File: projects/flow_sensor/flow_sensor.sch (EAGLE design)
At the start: 89 parts, among them IC1 TPS61200, IC2 TPS61200, IC3 MIC5219BM5, J5 455-1750-1-ND

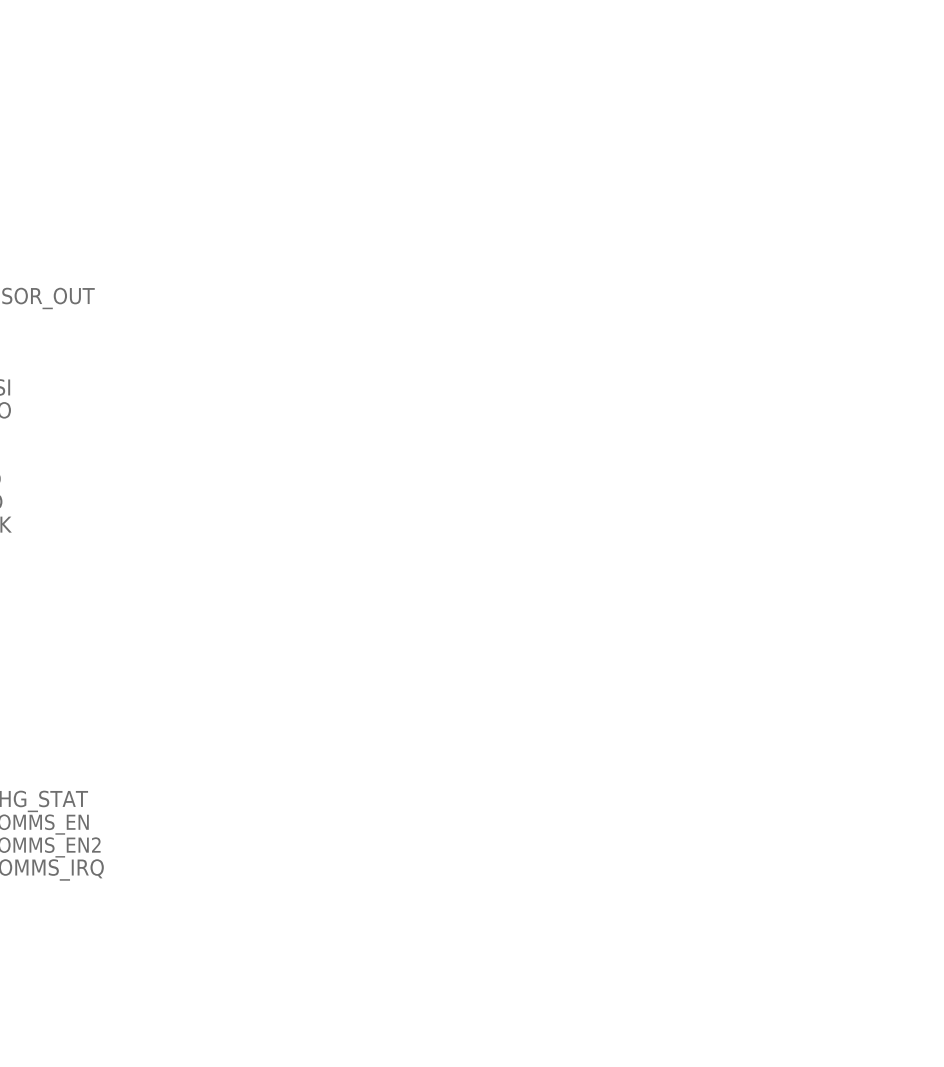
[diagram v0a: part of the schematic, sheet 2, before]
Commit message: Added MSP430F5229 to replace MSP430FR5994
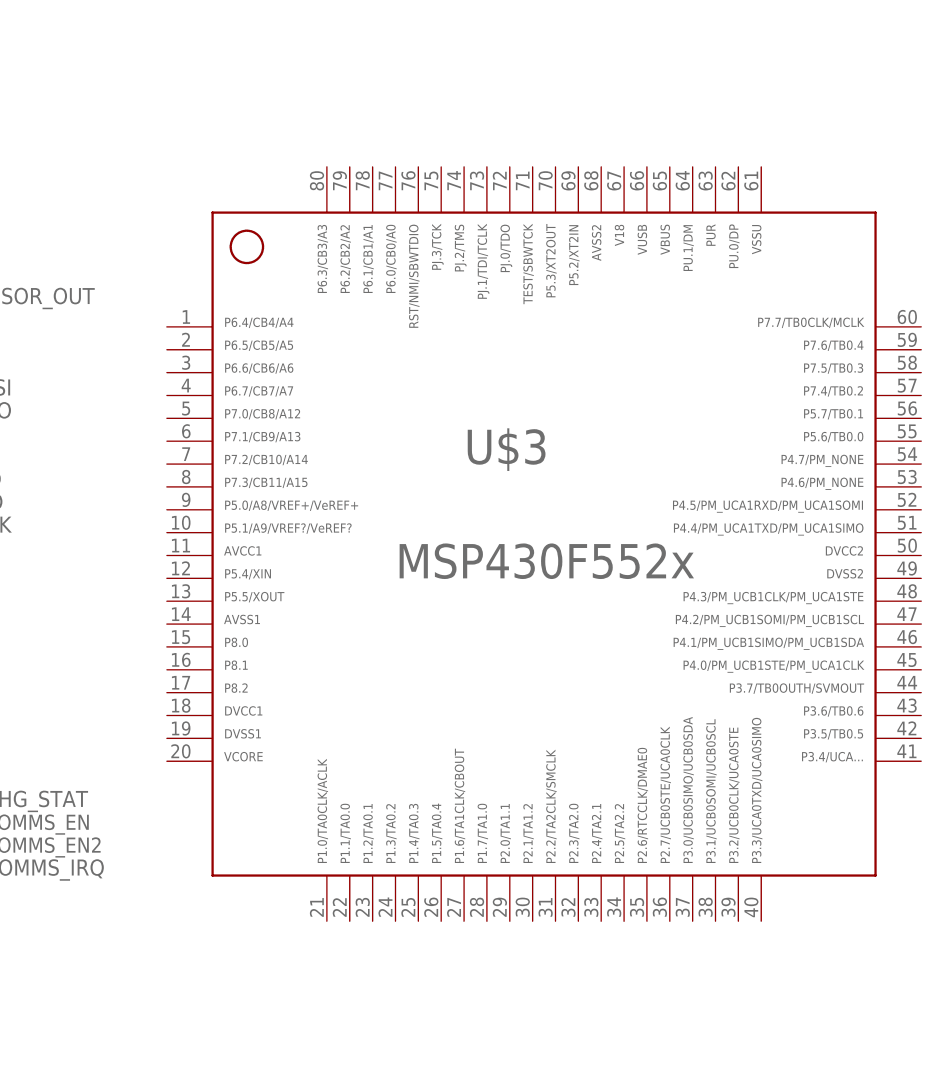
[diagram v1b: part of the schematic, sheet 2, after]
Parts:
- added U$3: F552X---PN80, TI_MSP430_v16:F552X---PN80
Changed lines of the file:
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@@
 <part name="J4" library="SparkFun-Connectors" deviceset="CONN_02" device="1X02_NO_SILK"/>
 <part name="R11" library="SparkFun-Resistors" deviceset="180OHM" device="-0603-1/10W-1%" value="180k"/>
+<part name="U$3" library="TI_MSP430_v16" deviceset="F552X---PN80" device=""/>
 </parts>
 <sheets>
@@
 <instance part="C44" gate="G$1" x="203.2" y="15.24" rot="R180"/>
 <instance part="GND42" gate="1" x="203.2" y="5.08"/>
+<instance part="U$3" gate="G$1" x="388.62" y="12.7"/>
 </instances>
 <busses>

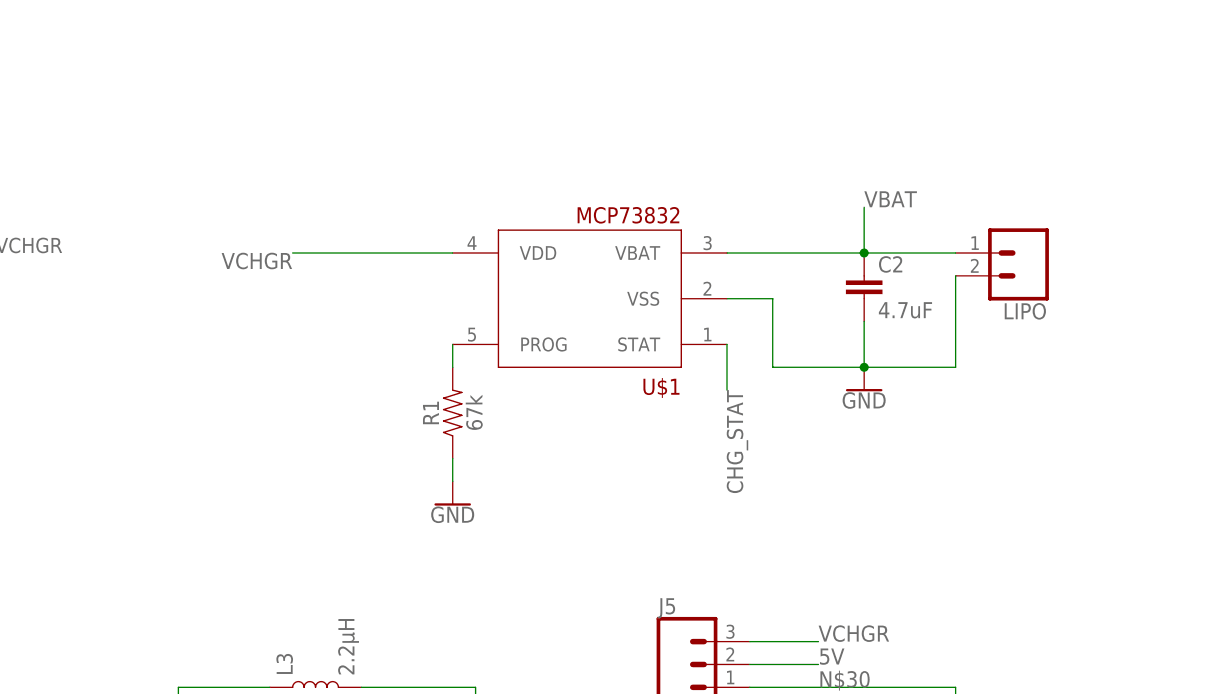
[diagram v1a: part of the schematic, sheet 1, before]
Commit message: Added XC6805 battery charger to replace mcp73832
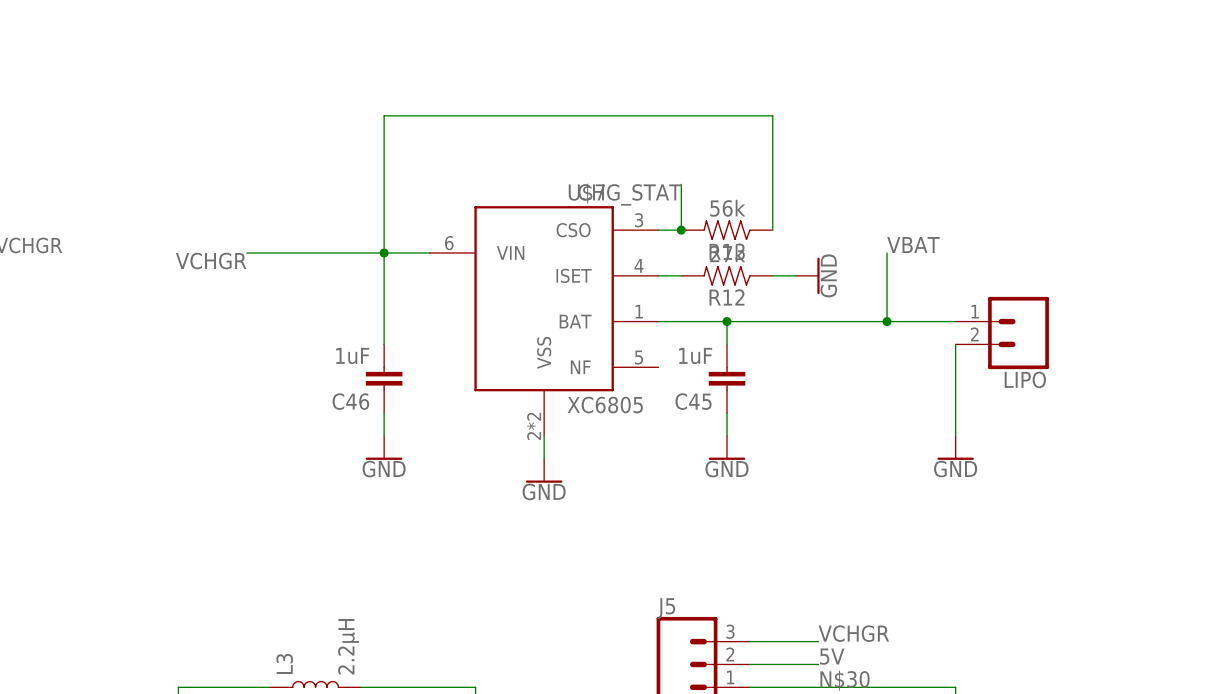
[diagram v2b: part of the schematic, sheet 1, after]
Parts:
- removed C2: 4.7uF, SparkFun-Capacitors:4.7UF0603
- removed R1: 67k, SparkFun-Resistors:20KOHM-0603-1/10W-1%
- removed U$1: MCP73832, my_library:MCP73832
- added C45, C46: 1uF, SparkFun-Capacitors:4.7UF0603
- added R12: 27k, SparkFun-Resistors:20KOHM-0603-1/10W-1%
- added R13: 56k, SparkFun-Resistors:20KOHM-0603-1/10W-1%
- added U$7: XC6805, my_library:XC6805
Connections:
- removed net N$2: R1.2, U$1.PROG
- new net N$39: R12.2, U$7.ISET
- net CHG_STAT: now also R13.2, U$7.CSO; no longer U$1.STAT
- net GND: now also C45.1, C46.1, R12.1, U$7.VSS; no longer C2.2, R1.1, U$1.VSS
- net VBAT: now also C45.2, U$7.BAT; no longer C2.1, U$1.VBAT
- net VCHGR: now also C46.2, R13.1, U$7.VIN; no longer U$1.VDD
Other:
- moved on the sheet: LIPO
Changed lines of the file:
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@@
 <attribute name="DESIGNER" value="A Osborn, M Silvern, N Yokley"/>
 </part>
-<part name="U$1" library="my_library" deviceset="MCP73832" device=""/>
-<part name="C2" library="SparkFun-Capacitors" deviceset="4.7UF" device="0603" value="4.7uF"/>
 <part name="LIPO" library="SparkFun-Connectors" deviceset="CONN_02" device="1X02_NO_SILK"/>
-<part name="R1" library="SparkFun-Resistors" deviceset="20KOHM" device="-0603-1/10W-1%" value="67k"/>
 <part name="FRAME3" library="SparkFun-Aesthetics" deviceset="FRAME-A4L" device="">
 <attribute name="CNAME" value="Communications"/>
@@
 <part name="GND31" library="SparkFun-PowerSymbols" deviceset="GND" device=""/>
 <part name="GND32" library="SparkFun-PowerSymbols" deviceset="GND" device=""/>
-<part name="GND1" library="SparkFun-PowerSymbols" deviceset="GND" device=""/>
-<part name="GND2" library="SparkFun-PowerSymbols" deviceset="GND" device=""/>
 <part name="GND21" library="SparkFun-PowerSymbols" deviceset="GND" device=""/>
 <part name="GND25" library="SparkFun-PowerSymbols" deviceset="GND" device=""/>
@@
 <part name="R11" library="SparkFun-Resistors" deviceset="180OHM" device="-0603-1/10W-1%" value="180k"/>
 <part name="U$3" library="TI_MSP430_v16" deviceset="F552X---PN80" device=""/>
+<part name="U$7" library="my_library" deviceset="XC6805" device=""/>
+<part name="GND24" library="SparkFun-PowerSymbols" deviceset="GND" device=""/>
+<part name="R12" library="SparkFun-Resistors" deviceset="20KOHM" device="-0603-1/10W-1%" value="27k"/>
+<part name="GND43" library="SparkFun-PowerSymbols" deviceset="GND" device=""/>
+<part name="C45" library="SparkFun-Capacitors" deviceset="4.7UF" device="0603" value="1uF"/>
+<part name="GND44" library="SparkFun-PowerSymbols" deviceset="GND" device=""/>
+<part name="C46" library="SparkFun-Capacitors" deviceset="4.7UF" device="0603" value="1uF"/>
+<part name="GND45" library="SparkFun-PowerSymbols" deviceset="GND" device=""/>
+<part name="R13" library="SparkFun-Resistors" deviceset="20KOHM" device="-0603-1/10W-1%" value="56k"/>
+<part name="GND1" library="SparkFun-PowerSymbols" deviceset="GND" device=""/>
 </parts>
 <sheets>
@@
 <attribute name="CREVISION" x="-139.7" y="-91.44" size="1.778" layer="96" display="off"/>
 </instance>
-<instance part="U$1" gate="G$1" x="45.72" y="58.42" rot="R180"/>
-<instance part="C2" gate="G$1" x="76.2" y="58.42"/>
-<instance part="LIPO" gate="G$1" x="93.98" y="63.5" rot="R180"/>
-<instance part="R1" gate="G$1" x="30.48" y="45.72" rot="R90"/>
+<instance part="LIPO" gate="G$1" x="93.98" y="55.88" rot="R180"/>
 <instance part="IC1" gate="G$1" x="17.78" y="-10.16"/>
 <instance part="L3" gate="G$1" x="15.24" y="15.24" rot="R90"/>
@@
 <instance part="GND31" gate="1" x="101.6" y="-27.94"/>
 <instance part="GND32" gate="1" x="88.9" y="-27.94"/>
-<instance part="GND1" gate="1" x="76.2" y="48.26"/>
-<instance part="GND2" gate="1" x="30.48" y="35.56"/>
 <instance part="GND21" gate="1" x="233.68" y="40.64" rot="R90"/>
 <instance part="GND25" gate="1" x="279.4" y="58.42" rot="R90"/>
@@
 <instance part="J4" gate="G$1" x="177.8" y="50.8"/>
 <instance part="R11" gate="G$1" x="81.28" y="-17.78" rot="R90"/>
+<instance part="U$7" gate="G$1" x="40.64" y="58.42"/>
+<instance part="GND24" gate="1" x="40.64" y="38.1"/>
+<instance part="R12" gate="G$1" x="60.96" y="60.96" rot="R180"/>
+<instance part="GND43" gate="1" x="71.12" y="60.96" rot="R90"/>
+<instance part="C45" gate="G$1" x="60.96" y="50.8" rot="R180"/>
+<instance part="GND44" gate="1" x="60.96" y="40.64"/>
+<instance part="C46" gate="G$1" x="22.86" y="50.8" rot="R180"/>
+<instance part="GND45" gate="1" x="22.86" y="40.64"/>
+<instance part="R13" gate="G$1" x="60.96" y="66.04" rot="R180"/>
+<instance part="GND1" gate="1" x="86.36" y="40.64"/>
 </instances>
 <busses>
@@
 <nets>
 <net name="GND" class="0">
-<segment>
-<pinref part="C2" gate="G$1" pin="2"/>
-<wire x1="76.2" y1="55.88" x2="76.2" y2="50.8" width="0.1524" layer="91"/>
-<pinref part="LIPO" gate="G$1" pin="2"/>
-<wire x1="86.36" y1="60.96" x2="86.36" y2="50.8" width="0.1524" layer="91"/>
-<wire x1="86.36" y1="50.8" x2="76.2" y2="50.8" width="0.1524" layer="91"/>
-<junction x="76.2" y="50.8"/>
-<pinref part="U$1" gate="G$1" pin="VSS"/>
-<wire x1="60.96" y1="58.42" x2="66.04" y2="58.42" width="0.1524" layer="91"/>
-<wire x1="66.04" y1="58.42" x2="66.04" y2="50.8" width="0.1524" layer="91"/>
-<wire x1="66.04" y1="50.8" x2="76.2" y2="50.8" width="0.1524" layer="91"/>
-<pinref part="GND1" gate="1" pin="GND"/>
-</segment>
-<segment>
-<pinref part="R1" gate="G$1" pin="1"/>
-<wire x1="30.48" y1="38.1" x2="30.48" y2="40.64" width="0.1524" layer="91"/>
-<pinref part="GND2" gate="1" pin="GND"/>
-</segment>
 <segment>
 <pinref part="R7" gate="G$1" pin="1"/>
@@
 <wire x1="208.28" y1="-12.7" x2="208.28" y2="-10.16" width="0.1524" layer="91"/>
 </segment>
+<segment>
+<pinref part="U$7" gate="G$1" pin="VSS"/>
+<pinref part="GND24" gate="1" pin="GND"/>
+<wire x1="40.64" y1="40.64" x2="40.64" y2="43.18" width="0.1524" layer="91"/>
+</segment>
+<segment>
+<pinref part="R12" gate="G$1" pin="1"/>
+<pinref part="GND43" gate="1" pin="GND"/>
+<wire x1="68.58" y1="60.96" x2="66.04" y2="60.96" width="0.1524" layer="91"/>
+</segment>
+<segment>
+<pinref part="GND44" gate="1" pin="GND"/>
+<pinref part="C45" gate="G$1" pin="1"/>
+<wire x1="60.96" y1="43.18" x2="60.96" y2="45.72" width="0.1524" layer="91"/>
+</segment>
+<segment>
+<pinref part="C46" gate="G$1" pin="1"/>
+<pinref part="GND45" gate="1" pin="GND"/>
+<wire x1="22.86" y1="43.18" x2="22.86" y2="45.72" width="0.1524" layer="91"/>
+</segment>
+<segment>
+<pinref part="LIPO" gate="G$1" pin="2"/>
+<wire x1="86.36" y1="53.34" x2="86.36" y2="43.18" width="0.1524" layer="91"/>
+<pinref part="GND1" gate="1" pin="GND"/>
+</segment>
 </net>
 <net name="CHG_STAT" class="0">
 <segment>
-<pinref part="U$1" gate="G$1" pin="STAT"/>
-<wire x1="60.96" y1="53.34" x2="60.96" y2="48.26" width="0.1524" layer="91"/>
-<label x="60.96" y="48.26" size="1.778" layer="95" rot="R270"/>
+<pinref part="U$7" gate="G$1" pin="CSO"/>
+<pinref part="R13" gate="G$1" pin="2"/>
+<wire x1="53.34" y1="66.04" x2="55.88" y2="66.04" width="0.1524" layer="91"/>
+<wire x1="55.88" y1="66.04" x2="55.88" y2="71.12" width="0.1524" layer="91"/>
+<junction x="55.88" y="66.04"/>
+<label x="55.88" y="71.12" size="1.778" layer="95" rot="R180"/>
 </segment>
 </net>
 <net name="VBAT" class="0">
-<segment>
-<pinref part="U$1" gate="G$1" pin="VBAT"/>
-<wire x1="60.96" y1="63.5" x2="76.2" y2="63.5" width="0.1524" layer="91"/>
-<pinref part="C2" gate="G$1" pin="1"/>
-<pinref part="LIPO" gate="G$1" pin="1"/>
-<wire x1="86.36" y1="63.5" x2="76.2" y2="63.5" width="0.1524" layer="91"/>
-<junction x="76.2" y="63.5"/>
-<wire x1="76.2" y1="63.5" x2="76.2" y2="68.58" width="0.1524" layer="91"/>
-<label x="76.2" y="68.58" size="1.778" layer="95"/>
-</segment>
 <segment>
 <pinref part="IC1" gate="G$1" pin="VIN"/>
@@
 <wire x1="0" y1="15.24" x2="10.16" y2="15.24" width="0.1524" layer="91"/>
 </segment>
-</net>
-<net name="N$2" class="0">
-<segment>
-<pinref part="U$1" gate="G$1" pin="PROG"/>
-<pinref part="R1" gate="G$1" pin="2"/>
-<wire x1="30.48" y1="50.8" x2="30.48" y2="53.34" width="0.1524" layer="91"/>
+<segment>
+<pinref part="U$7" gate="G$1" pin="BAT"/>
+<wire x1="53.34" y1="55.88" x2="60.96" y2="55.88" width="0.1524" layer="91"/>
+<pinref part="C45" gate="G$1" pin="2"/>
+<wire x1="60.96" y1="55.88" x2="60.96" y2="53.34" width="0.1524" layer="91"/>
+<junction x="60.96" y="55.88"/>
+<label x="78.74" y="63.5" size="1.778" layer="95"/>
+<pinref part="LIPO" gate="G$1" pin="1"/>
+<wire x1="60.96" y1="55.88" x2="78.74" y2="55.88" width="0.1524" layer="91"/>
+<wire x1="78.74" y1="55.88" x2="86.36" y2="55.88" width="0.1524" layer="91"/>
+<wire x1="78.74" y1="55.88" x2="78.74" y2="63.5" width="0.1524" layer="91"/>
+<junction x="78.74" y="55.88"/>
 </segment>
 </net>
@@
 </net>
 <net name="VCHGR" class="0">
-<segment>
-<pinref part="U$1" gate="G$1" pin="VDD"/>
-<label x="12.7" y="63.5" size="1.778" layer="95" rot="R180"/>
-<wire x1="12.7" y1="63.5" x2="30.48" y2="63.5" width="0.1524" layer="91"/>
-</segment>
 <segment>
 <pinref part="IC2" gate="G$1" pin="VOUT"/>
@@
 <wire x1="63.5" y1="20.32" x2="71.12" y2="20.32" width="0.1524" layer="91"/>
 <label x="71.12" y="20.32" size="1.778" layer="95"/>
+</segment>
+<segment>
+<label x="7.62" y="63.5" size="1.778" layer="95" rot="R180"/>
+<pinref part="C46" gate="G$1" pin="2"/>
+<wire x1="22.86" y1="53.34" x2="22.86" y2="63.5" width="0.1524" layer="91"/>
+<wire x1="22.86" y1="63.5" x2="7.62" y2="63.5" width="0.1524" layer="91"/>
+<pinref part="U$7" gate="G$1" pin="VIN"/>
+<wire x1="22.86" y1="63.5" x2="27.94" y2="63.5" width="0.1524" layer="91"/>
+<junction x="22.86" y="63.5"/>
+<pinref part="R13" gate="G$1" pin="1"/>
+<wire x1="66.04" y1="66.04" x2="66.04" y2="78.74" width="0.1524" layer="91"/>
+<wire x1="66.04" y1="78.74" x2="22.86" y2="78.74" width="0.1524" layer="91"/>
+<wire x1="22.86" y1="78.74" x2="22.86" y2="63.5" width="0.1524" layer="91"/>
 </segment>
 </net>
@@
 </segment>
 </net>
+<net name="N$39" class="0">
+<segment>
+<pinref part="U$7" gate="G$1" pin="ISET"/>
+<pinref part="R12" gate="G$1" pin="2"/>
+<wire x1="55.88" y1="60.96" x2="53.34" y2="60.96" width="0.1524" layer="91"/>
+</segment>
+</net>
